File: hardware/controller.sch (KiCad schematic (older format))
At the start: 76 parts, among them J1 USB_B_Micro, Q1 AO3402, Q2 AO3401A, Q3 AO3402, SW1 SW_Push_NO_NC_LED, SW10 SW_Push_NO_NC_LED, SW11 SW_Push_NO_NC_LED, SW12 SW_Push_NO_NC_LED, SW13 SW_Push_NO_NC_LED, SW14 SW_Push_NO_NC_LED, SW15 SW_Push_NO_NC_LED, SW16 SW_Push_NO_NC_LED, SW2 SW_Push_NO_NC_LED, SW3 SW_Push_NO_NC_LED, SW4 SW_Push_NO_NC_LED, SW5 SW_Push_NO_NC_LED, SW6 SW_Push_NO_NC_LED, SW7 SW_Push_NO_NC_LED, SW8 SW_Push_NO_NC_LED, SW9 SW_Push_NO_NC_LED, U1 ESP-12F, U2 ME6211C33M5G, U3 MCP23017_SS, U4 CH340C, U5 PCA9685PW

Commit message: use ATmega8, add PCB (before automatic rounting)
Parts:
- removed C10: 10u, Capacitor_SMD:C_0805_2012Metric, symbol Device:C_Small
- removed C4: 1u, Capacitor_SMD:C_0805_2012Metric, symbol Device:C_Small
- removed H2, H3: MountingHole_Pad, MountingHole:MountingHole_3.5mm_Pad_Via, symbol Mechanical:MountingHole_Pad
- removed Q2: AO3401A, Package_TO_SOT_SMD:SOT-23, symbol Device:Q_PMOS_GSD
- removed R1, R2: 10k, Resistor_SMD:R_0805_2012Metric, symbol Device:R
- removed R10, R11, R12, R13, R14, R15, R16, R17, R18, R19, R20, R21, R22, R24, R25, R7, R8, R9: 470, Resistor_SMD:R_0805_2012Metric, symbol Device:R
- removed TP1: TXD, TestPoint:TestPoint_Loop_D1.80mm_Drill1.0mm_Beaded, symbol Connector:TestPoint
- removed TP2: RXD, TestPoint:TestPoint_Loop_D1.80mm_Drill1.0mm_Beaded, symbol Connector:TestPoint
- removed TP3: GPIO0, TestPoint:TestPoint_Loop_D1.80mm_Drill1.0mm_Beaded, symbol Connector:TestPoint
- removed TP4: ~RST, TestPoint:TestPoint_Loop_D1.80mm_Drill1.0mm_Beaded, symbol Connector:TestPoint
- removed TP5: ~RTS, TestPoint:TestPoint_Loop_D1.80mm_Drill1.0mm_Beaded, symbol Connector:TestPoint
- removed TP6: ~DTR, TestPoint:TestPoint_Loop_D1.80mm_Drill1.0mm_Beaded, symbol Connector:TestPoint
- removed U1: ESP-12F, RF_Module:ESP-12E, symbol RF_Module:ESP-12F
- removed U2: ME6211C33M5G, Package_TO_SOT_SMD:SOT-23-5, symbol Regulator_Linear:TLV75533PDBV
- added C2, C5: 100n, Capacitor_SMD:C_0805_2012Metric, symbol Device:C_Small
- added H2, H3, H4: MountingHole, MountingHole:MountingHole_3.5mm, symbol Mechanical:MountingHole
- added J2: AVR-ISP-6, Connector_PinHeader_2.54mm:PinHeader_2x03_P2.54mm_Vertical, symbol Connector:AVR-ISP-6
- added Q10, Q11, Q12, Q13, Q14, Q15, Q16, Q2, Q4, Q5, Q6, Q7, Q8, Q9: AO3402, Package_TO_SOT_SMD:SOT-23, symbol Device:Q_NMOS_GSD
- added U2: ATmega328-AU, Package_QFP:TQFP-32_7x7mm_P0.8mm, symbol MCU_Microchip_ATmega:ATmega328-AU
- added Y1: 14.7456 Mhz, Crystal:Crystal_SMD_HC49-SD, symbol Device:Crystal
- C1: footprint Capacitor_SMD:C_0805_2012Metric -> Capacitor_THT:C_Disc_D6.0mm_W2.5mm_P5.00mm
- C3: value 1u -> 100n
- C6: value 10u -> 100n
- C7: value 10u -> 22p
- C8: value 100n -> 22p
- H1: value MountingHole_Pad -> MountingHole; footprint MountingHole:MountingHole_3.5mm_Pad_Via -> MountingHole:MountingHole_3.5mm; symbol Mechanical:MountingHole_Pad -> Mechanical:MountingHole
- renumbered C9 to C10, C2 to C4, C5 to C9, R23 to R1, R6 to R2, TP7 to TP1, TP8 to TP2, TP9 to TP3, TP10 to TP4, TP11 to TP5, TP12 to TP6, U4 to U1, U5 to U4
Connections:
- net labels added: BTNx0, BTNx1, BTNx2, BTNx3, BTNx4, BTNx5, BTNx6, BTNx7, BTNx8, BTNx9, BTNxA, BTNxB, BTNxC, BTNxD, BTNxE, BTNxF, INTA, INTB, LEDx0, LEDx1, LEDx2, LEDx3, LEDx4, LEDx5, LEDx6, LEDx7, LEDx8, LEDx9, LEDxA, LEDxB, LEDxC, LEDxD, LEDxE, LEDxF, MCP23017.~RESET, MISO, MOSI, PCA9685.~OE, SCK, XTAL1, XTAL2
- net labels removed: +3V3, BTNx0#-, BTNx0#C, BTNx1#-, BTNx1#C, BTNx2#-, BTNx2#C, BTNx3#-, BTNx3#C, BTNx4#-, BTNx4#C, BTNx5#-, BTNx5#C, BTNx6#-, BTNx6#C, BTNx7#-, BTNx7#C, BTNx8#-, BTNx8#C, BTNx9#-, BTNx9#C, BTNxA#-, BTNxA#C, BTNxB#-, BTNxB#C, BTNxC#-, BTNxC#C, BTNxD#-, BTNxD#C, BTNxE#-, BTNxE#C, BTNxF#-, BTNxF#C, GPIO0, ~DTR, ~OE, ~RTS
- wire segments 353 -> 290
- no-connect marks 34 -> 40
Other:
- note removed: "nRTS / nDTR -> nRST / GPIO0\nL / L -> H / H\nL / H -> L / H\nH / L -> H / L\nH / H -> H / H"
- moved on the sheet: C10, C4, C9, F1, J1, R1, R2, TP1, TP2, TP3, TP4, TP5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

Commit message: fix pull-up resistors: MCP23017.~RESET is always pulled high; PCA9685.~OE is pulled high but can be driven low by PC2
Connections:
- wire segments 290 -> 289
- no-connect marks 40 -> 41
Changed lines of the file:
@@
 Wire Wire Line
 	6550 2950 6600 2950
-Text GLabel 6600 2950 2    33   Output ~ 0
-MCP23017.~RESET
 Wire Wire Line
 	4850 4050 4900 4050
-Text GLabel 6600 3050 2    33   Output ~ 0
-PCA9685.~OE
-Wire Wire Line
-	6550 3050 6600 3050
 Wire Wire Line
 	3650 1750 3700 1750
@@
 Wire Wire Line
 	7250 4150 7300 4150
-$Comp
-L power:GND #PWR073
-U 1 1 5E980FCC
-P 10100 5500
-F 0 "#PWR073" H 10100 5250 50  0001 C CNN
-F 1 "GND" H 10105 5327 50  0000 C CNN
-F 2 "" H 10100 5500 50  0001 C CNN
-F 3 "" H 10100 5500 50  0001 C CNN
-	1    10100 5500
-	1    0    0    -1
-$EndComp
 Wire Wire Line
 	10400 5500 10400 5450
@@
 Wire Wire Line
 	9800 5450 9800 5500
-Wire Wire Line
-	9200 5450 9200 5500
-Wire Wire Line
-	9500 5450 9500 5500
-Wire Wire Line
-	10100 5500 10100 5450
 $Comp
 L power:+5V #PWR074
@@
 	1    0    0    -1
 $EndComp
-Wire Wire Line
-	10100 5100 10100 5150
-$Comp
-L Device:R R4
-U 1 1 612CD065
-P 10100 5300
-F 0 "R4" H 10030 5254 50  0000 R CNN
-F 1 "10k" H 10030 5345 50  0000 R CNN
-F 2 "Resistor_SMD:R_0805_2012Metric" V 10030 5300 50  0001 C CNN
-F 3 "~" H 10100 5300 50  0001 C CNN
-	1    10100 5300
-	-1   0    0    1
-$EndComp
-Text GLabel 10100 5100 1    33   UnSpc ~ 0
-MCP23017.~RESET
 Wire Wire Line
 	9800 5100 9800 5150
@@
 ~RST
 $Comp
-L power:+5V #PWR069
-U 1 1 5ED52F54
-P 9200 5100
-F 0 "#PWR069" H 9200 4950 50  0001 C CNN
-F 1 "+5V" H 9215 5273 50  0000 C CNN
-F 2 "" H 9200 5100 50  0001 C CNN
-F 3 "" H 9200 5100 50  0001 C CNN
-	1    9200 5100
-	1    0    0    -1
-$EndComp
-$Comp
-L power:+5V #PWR070
-U 1 1 5ED51F9D
-P 9500 5100
-F 0 "#PWR070" H 9500 4950 50  0001 C CNN
-F 1 "+5V" H 9515 5273 50  0000 C CNN
-F 2 "" H 9500 5100 50  0001 C CNN
-F 3 "" H 9500 5100 50  0001 C CNN
-	1    9500 5100
-	1    0    0    -1
-$EndComp
-Text GLabel 9500 5500 3    50   UnSpc ~ 0
-SDA
-Text GLabel 9200 5500 3    50   UnSpc ~ 0
-SCL
-Wire Wire Line
-	9200 5100 9200 5150
-Wire Wire Line
-	9500 5100 9500 5150
+L Device:C_Small C7
+U 1 1 601D1409
+P 7300 4350
+F 0 "C7" H 7415 4396 50  0000 L CNN
+F 1 "22p" H 7415 4305 50  0000 L CNN
+F 2 "Capacitor_SMD:C_0805_2012Metric" H 7338 4200 50  0001 C CNN
+F 3 "~" H 7300 4350 50  0001 C CNN
+	1    7300 4350
+	1    0    0    -1
+$EndComp
+Text GLabel 6600 2550 2    50   Output ~ 0
+XTAL2
+Wire Wire Line
+	6550 2550 6600 2550
+Text GLabel 6600 2450 2    50   Input ~ 0
+XTAL1
+Wire Wire Line
+	6600 2450 6550 2450
+$Comp
+L Device:R R2
+U 1 1 5E2A6C3C
+P 9500 5300
+F 0 "R2" H 9430 5254 50  0000 R CNN
+F 1 "1k5" H 9430 5345 50  0000 R CNN
+F 2 "Resistor_SMD:R_0805_2012Metric" V 9430 5300 50  0001 C CNN
+F 3 "~" H 9500 5300 50  0001 C CNN
+	1    9500 5300
+	-1   0    0    1
+$EndComp
 $Comp
 L Device:R R1
@@
 	-1   0    0    1
 $EndComp
-$Comp
-L Device:R R2
-U 1 1 5E2A6C3C
-P 9500 5300
-F 0 "R2" H 9430 5254 50  0000 R CNN
-F 1 "1k5" H 9430 5345 50  0000 R CNN
-F 2 "Resistor_SMD:R_0805_2012Metric" V 9430 5300 50  0001 C CNN
-F 3 "~" H 9500 5300 50  0001 C CNN
-	1    9500 5300
-	-1   0    0    1
-$EndComp
-$Comp
-L Device:C_Small C7
-U 1 1 601D1409
-P 7300 4350
-F 0 "C7" H 7415 4396 50  0000 L CNN
-F 1 "22p" H 7415 4305 50  0000 L CNN
-F 2 "Capacitor_SMD:C_0805_2012Metric" H 7338 4200 50  0001 C CNN
-F 3 "~" H 7300 4350 50  0001 C CNN
-	1    7300 4350
-	1    0    0    -1
-$EndComp
-Text GLabel 6600 2550 2    50   Output ~ 0
-XTAL2
-Wire Wire Line
-	6550 2550 6600 2550
-Text GLabel 6600 2450 2    50   Input ~ 0
-XTAL1
-Wire Wire Line
-	6600 2450 6550 2450
+Wire Wire Line
+	9500 5100 9500 5150
+Wire Wire Line
+	9200 5100 9200 5150
+Text GLabel 9200 5500 3    50   UnSpc ~ 0
+SCL
+Text GLabel 9500 5500 3    50   UnSpc ~ 0
+SDA
+$Comp
+L power:+5V #PWR070
+U 1 1 5ED51F9D
+P 9500 5100
+F 0 "#PWR070" H 9500 4950 50  0001 C CNN
+F 1 "+5V" H 9515 5273 50  0000 C CNN
+F 2 "" H 9500 5100 50  0001 C CNN
+F 3 "" H 9500 5100 50  0001 C CNN
+	1    9500 5100
+	1    0    0    -1
+$EndComp
+$Comp
+L power:+5V #PWR069
+U 1 1 5ED52F54
+P 9200 5100
+F 0 "#PWR069" H 9200 4950 50  0001 C CNN
+F 1 "+5V" H 9215 5273 50  0000 C CNN
+F 2 "" H 9200 5100 50  0001 C CNN
+F 3 "" H 9200 5100 50  0001 C CNN
+	1    9200 5100
+	1    0    0    -1
+$EndComp
+Wire Wire Line
+	9500 5450 9500 5500
+Wire Wire Line
+	9200 5450 9200 5500
+Text GLabel 6600 2950 2    33   Output ~ 0
+PCA9685.~OE
+Wire Wire Line
+	10100 5100 10100 5150
+Wire Wire Line
+	10100 5500 10100 5450
+$Comp
+L Device:R R4
+U 1 1 612CD065
+P 10100 5300
+F 0 "R4" H 10030 5254 50  0000 R CNN
+F 1 "10k" H 10030 5345 50  0000 R CNN
+F 2 "Resistor_SMD:R_0805_2012Metric" V 10030 5300 50  0001 C CNN
+F 3 "~" H 10100 5300 50  0001 C CNN
+	1    10100 5300
+	-1   0    0    -1
+$EndComp
+Text GLabel 10100 5500 3    33   UnSpc ~ 0
+MCP23017.~RESET
+$Comp
+L power:+5V #PWR?
+U 1 1 5EA7F4C0
+P 10100 5100
+F 0 "#PWR?" H 10100 4950 50  0001 C CNN
+F 1 "+5V" H 10115 5273 50  0000 C CNN
+F 2 "" H 10100 5100 50  0001 C CNN
+F 3 "" H 10100 5100 50  0001 C CNN
+	1    10100 5100
+	1    0    0    -1
+$EndComp
+NoConn ~ 6550 3050
 $EndSCHEMATC

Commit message: update schematic with separate connectors for LEDs and buttons
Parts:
- removed SW1, SW10, SW11, SW12, SW13, SW14, SW15, SW16, SW2, SW3, SW4, SW5, SW6, SW7, SW8, SW9: SW_Push_NO_NC_LED, Connector_Molex:Molex_PicoBlade_53047-0510_1x05_P1.25mm_Vertical, symbol controller:SW_Push_NO_NC_LED
- added J10, J11, J12, J13, J14, J15, J16, J17, J18, J3, J4, J5, J6, J7, J8, J9: Conn_01x02_Male, Connector_Molex:Molex_PicoBlade_53047-0210_1x02_P1.25mm_Vertical, symbol Connector:Conn_01x02_Male
- added J19, J20, J21, J22, J23, J24, J25, J26, J27, J28, J29, J30, J31, J32, J33, J34: Conn_01x03_Male, Connector_Molex:Molex_PicoBlade_53047-0310_1x03_P1.25mm_Vertical, symbol Connector:Conn_01x03_Male
- renumbered C3 to C1, C8 to C10, C4 to C2, C5 to C3, C6 to C4, C9 to C5, C10 to C6, C2 to C7, C1 to C8, C7 to C9, U4 to U2, U2 to U4
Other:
- moved on the sheet: C1, C10, C7, C8, C9, F1, H1, H2, H3, H4, J1, J2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

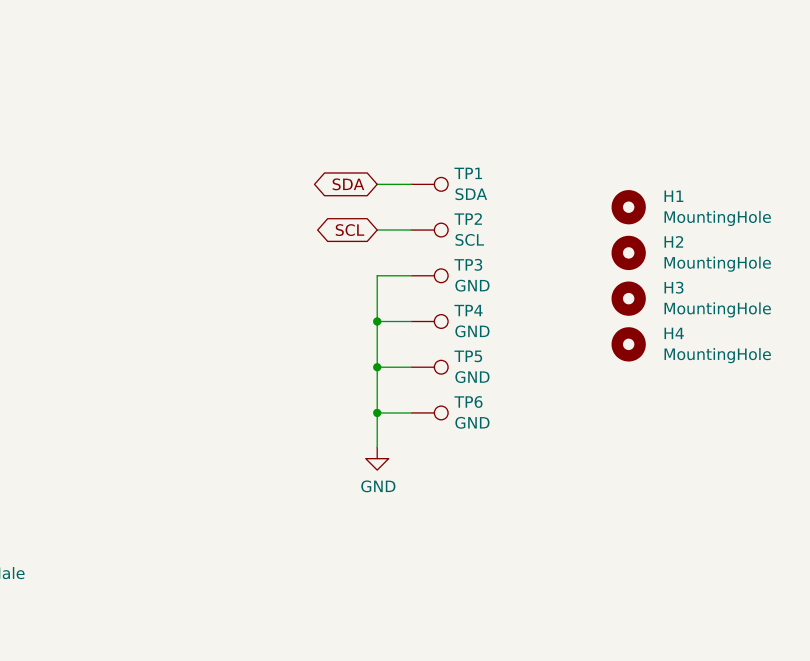
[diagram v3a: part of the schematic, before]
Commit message: remove test points
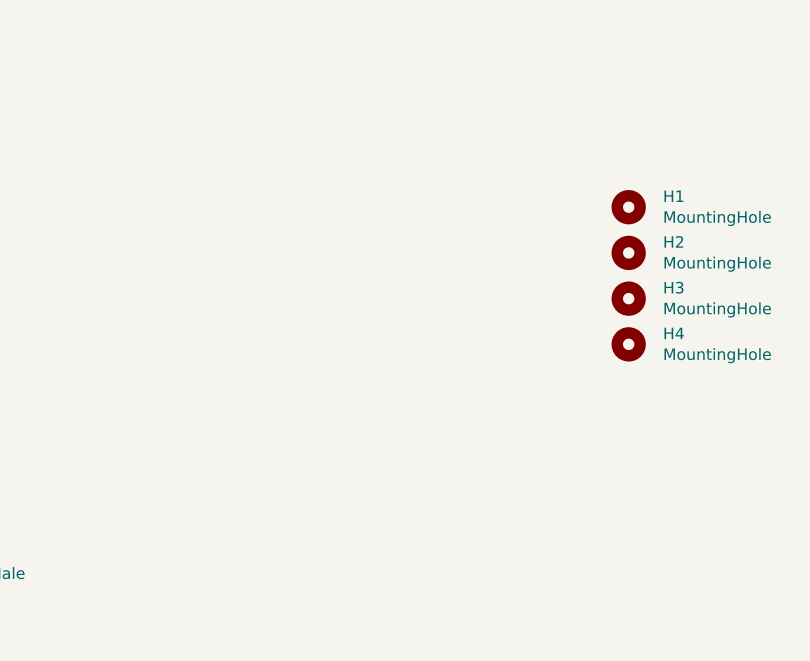
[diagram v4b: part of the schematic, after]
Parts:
- removed TP1: SDA, TestPoint:TestPoint_Loop_D1.80mm_Drill1.0mm_Beaded, symbol Connector:TestPoint
- removed TP2: SCL, TestPoint:TestPoint_Loop_D1.80mm_Drill1.0mm_Beaded, symbol Connector:TestPoint
- removed TP3, TP4, TP5, TP6: GND, TestPoint:TestPoint_Loop_D1.80mm_Drill1.0mm_Beaded, symbol Connector:TestPoint
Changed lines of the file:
@@
 Wire Wire Line
 	10050 3350 10050 3250
-Wire Wire Line
-	11850 8350 11850 8550
-Text GLabel 11850 7750 0    50   BiDi ~ 0
-SCL
-Text GLabel 11850 7550 0    50   BiDi ~ 0
-SDA
-$Comp
-L Connector:TestPoint TP2
-U 1 1 5E3F50CB
-P 12000 7750
-F 0 "TP2" V 11954 7938 50  0000 L CNN
-F 1 "SCL" V 12045 7938 50  0000 L CNN
-F 2 "TestPoint:TestPoint_Loop_D1.80mm_Drill1.0mm_Beaded" H 12200 7750 50  0001 C CNN
-F 3 "~" H 12200 7750 50  0001 C CNN
-	1    12000 7750
-	0    1    1    0
-$EndComp
-$Comp
-L Connector:TestPoint TP5
-U 1 1 5E7B1239
-P 12000 8350
-F 0 "TP5" V 11954 8538 50  0000 L CNN
-F 1 "GND" V 12045 8538 50  0000 L CNN
-F 2 "TestPoint:TestPoint_Loop_D1.80mm_Drill1.0mm_Beaded" H 12200 8350 50  0001 C CNN
-F 3 "~" H 12200 8350 50  0001 C CNN
-	1    12000 8350
-	0    1    1    0
-$EndComp
-Wire Wire Line
-	12000 8350 11850 8350
-Wire Wire Line
-	11850 7750 12000 7750
-Wire Wire Line
-	11850 7550 12000 7550
-$Comp
-L Connector:TestPoint TP1
-U 1 1 5E7B274E
-P 12000 7550
-F 0 "TP1" V 11954 7738 50  0000 L CNN
-F 1 "SDA" V 12045 7738 50  0000 L CNN
-F 2 "TestPoint:TestPoint_Loop_D1.80mm_Drill1.0mm_Beaded" H 12200 7550 50  0001 C CNN
-F 3 "~" H 12200 7550 50  0001 C CNN
-	1    12000 7550
-	0    1    1    0
-$EndComp
 Text Notes 11000 3650 0    50   ~ 0
 I2C Address: 0 1 0 0 (A2) (A1) (A0)
 $Comp
-L Connector:TestPoint TP6
-U 1 1 5EBCB80A
-P 12000 8550
-F 0 "TP6" V 11954 8738 50  0000 L CNN
-F 1 "GND" V 12045 8738 50  0000 L CNN
-F 2 "TestPoint:TestPoint_Loop_D1.80mm_Drill1.0mm_Beaded" H 12200 8550 50  0001 C CNN
-F 3 "~" H 12200 8550 50  0001 C CNN
-	1    12000 8550
-	0    1    1    0
-$EndComp
-Wire Wire Line
-	12000 8550 11850 8550
-$Comp
-L Connector:TestPoint TP4
-U 1 1 5E42C1D7
-P 12000 8150
-F 0 "TP4" V 11954 8338 50  0000 L CNN
-F 1 "GND" V 12045 8338 50  0000 L CNN
-F 2 "TestPoint:TestPoint_Loop_D1.80mm_Drill1.0mm_Beaded" H 12200 8150 50  0001 C CNN
-F 3 "~" H 12200 8150 50  0001 C CNN
-	1    12000 8150
-	0    1    1    0
-$EndComp
-$Comp
-L Connector:TestPoint TP3
-U 1 1 5E42D41F
-P 12000 7950
-F 0 "TP3" V 11954 8138 50  0000 L CNN
-F 1 "GND" V 12045 8138 50  0000 L CNN
-F 2 "TestPoint:TestPoint_Loop_D1.80mm_Drill1.0mm_Beaded" H 12200 7950 50  0001 C CNN
-F 3 "~" H 12200 7950 50  0001 C CNN
-	1    12000 7950
-	0    1    1    0
-$EndComp
-Wire Wire Line
-	11850 8350 11850 8150
-Wire Wire Line
-	11850 7950 12000 7950
-Connection ~ 11850 8350
-Wire Wire Line
-	12000 8150 11850 8150
-Connection ~ 11850 8150
-Wire Wire Line
-	11850 8150 11850 7950
-$Comp
-L power:GND #PWR068
-U 1 1 5E500BD6
-P 11850 8700
-F 0 "#PWR068" H 11850 8450 50  0001 C CNN
-F 1 "GND" H 11855 8527 50  0000 C CNN
-F 2 "" H 11850 8700 50  0001 C CNN
-F 3 "" H 11850 8700 50  0001 C CNN
-	1    11850 8700
-	1    0    0    -1
-$EndComp
-Wire Wire Line
-	11850 8700 11850 8550
-Connection ~ 11850 8550
-$Comp
 L power:+5V #PWR011

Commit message: create routing-friendly PCB layout and route it manually
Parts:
- removed J10, J11, J12, J13, J14, J15, J16, J17, J18, J3, J4, J5, J6, J7, J8, J9: Conn_01x02_Male, Connector_Molex:Molex_PicoBlade_53047-0210_1x02_P1.25mm_Vertical, symbol Connector:Conn_01x02_Male
- removed J20, J21, J22, J23, J24, J25, J26, J27, J28, J29, J30, J31, J32, J33, J34: Conn_01x03_Male, Connector_Molex:Molex_PicoBlade_53047-0310_1x03_P1.25mm_Vertical, symbol Connector:Conn_01x03_Male
- added J10, J11, J12, J13, J14, J15, J16, J17, J18, J4, J5, J6, J7, J8, J9: Conn_01x05_Male, Connector_JST:JST_XH_B5B-XH-A_1x05_P2.50mm_Vertical, symbol Connector:Conn_01x05_Male
- J3: renamed from J19; value Conn_01x03_Male -> Conn_01x05_Male; footprint Connector_Molex:Molex_PicoBlade_53047-0310_1x03_P1.25mm_Vertical -> Connector_JST:JST_XH_B5B-XH-A_1x05_P2.50mm_Vertical; symbol Connector:Conn_01x03_Male -> Connector:Conn_01x05_Male
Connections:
- net +5V: now also J3.5 (Pin_5), J10.5 (Pin_5), J11.5 (Pin_5), J12.5 (Pin_5), J13.5 (Pin_5), J14.5 (Pin_5), J15.5 (Pin_5), J16.5 (Pin_5), J17.5 (Pin_5), J18.5 (Pin_5), J4.5 (Pin_5), J5.5 (Pin_5), J6.5 (Pin_5), J7.5 (Pin_5), J8.5 (Pin_5), J9.5 (Pin_5)
- net BTNx0: now also J3.4 (Pin_4); no longer J3.2 (Pin_2)
- net BTNx1: now also J4.4 (Pin_4)
- net BTNx2: now also J5.4 (Pin_4)
- net BTNx3: now also J6.4 (Pin_4)
- net BTNx4: now also J7.4 (Pin_4)
- net BTNx5: now also J8.4 (Pin_4)
- net BTNx6: now also J9.4 (Pin_4)
- net BTNx7: now also J10.4 (Pin_4)
- net BTNx8: now also J11.4 (Pin_4)
- net BTNx9: now also J12.4 (Pin_4)
- net BTNxA: now also J13.4 (Pin_4)
- net BTNxB: now also J14.4 (Pin_4)
- net BTNxC: now also J15.4 (Pin_4)
- net BTNxD: now also J16.4 (Pin_4)
- net BTNxE: now also J17.4 (Pin_4)
- net BTNxF: now also J18.4 (Pin_4)
- net GND: now also J3.3 (Pin_3), J10.3 (Pin_3), J11.3 (Pin_3), J12.3 (Pin_3), J13.3 (Pin_3), J14.3 (Pin_3), J15.3 (Pin_3), J16.3 (Pin_3), J17.3 (Pin_3), J18.3 (Pin_3), J4.3 (Pin_3), J5.3 (Pin_3), J6.3 (Pin_3), J7.3 (Pin_3), J8.3 (Pin_3), J9.3 (Pin_3); no longer J3.1 (Pin_1)
- net at Q1.3 (D): now also J3.1 (Pin_1)
- net at Q2.3 (D): now also J4.1 (Pin_1)
- net at Q3.3 (D): now also J5.1 (Pin_1)
- net at Q4.3 (D): now also J6.1 (Pin_1)
- net at Q5.3 (D): now also J7.1 (Pin_1)
- net at Q6.3 (D): now also J8.1 (Pin_1)
- net at Q7.3 (D): now also J9.1 (Pin_1)
- net at Q8.3 (D): now also J10.1 (Pin_1)
- net at Q9.3 (D): now also J11.1 (Pin_1)
- net at Q10.3 (D): now also J12.1 (Pin_1)
- net at Q11.3 (D): now also J13.1 (Pin_1)
- net at Q12.3 (D): now also J14.1 (Pin_1)
- net at Q13.3 (D): now also J15.1 (Pin_1)
- net at Q14.3 (D): now also J16.1 (Pin_1)
- net at Q15.3 (D): now also J17.1 (Pin_1)
- net at Q16.3 (D): now also J18.1 (Pin_1)
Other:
- moved on the sheet: H1, H2, H3, H4, Q1, R1, R2, R3, R4, R5

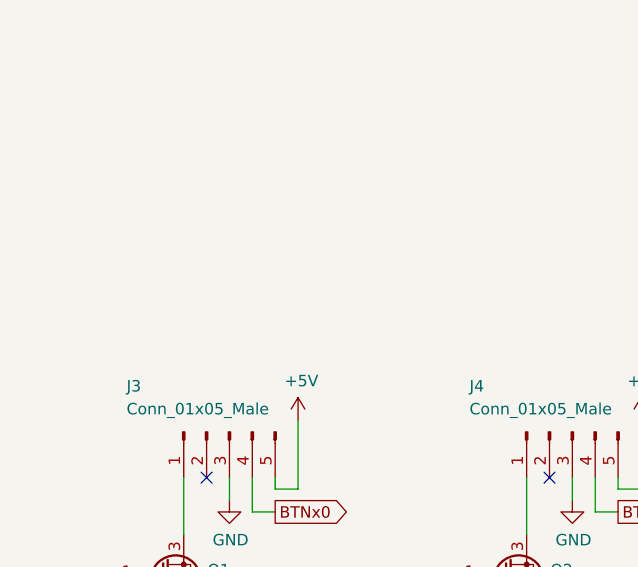
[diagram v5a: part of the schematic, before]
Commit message: change USB connector, finalize PCB shape
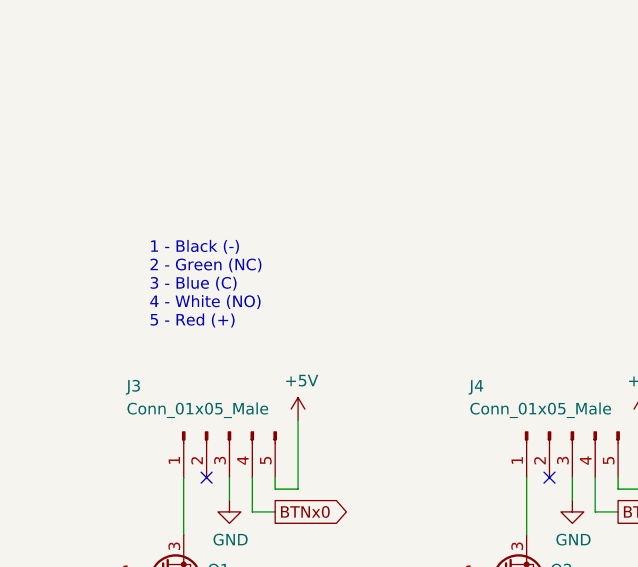
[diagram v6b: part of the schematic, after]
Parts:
- J1: footprint Connector_USB:USB_Micro-B_Amphenol_10103594-0001LF_Horizontal -> Connector_USB:USB_Micro-B_Molex-105017-0001
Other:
- note added: "1 - Black (-)\n2 - Green (NC)\n3 - Blue (C)\n4 - White (NO)\n5 - Red (+)\n"
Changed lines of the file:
@@
 F 0 "J1" H 1407 2417 50  0000 C CNN
 F 1 "USB_B_Micro" H 1407 2326 50  0000 C CNN
-F 2 "Connector_USB:USB_Micro-B_Amphenol_10103594-0001LF_Horizontal" H 1500 1900 50  0001 C CNN
+F 2 "Connector_USB:USB_Micro-B_Molex-105017-0001" H 1500 1900 50  0001 C CNN
 F 3 "~" H 1500 1900 50  0001 C CNN
 	1    1350 1950
@@
 	0    -1   1    0
 $EndComp
+Text Notes 1250 6300 0    50   ~ 0
+1 - Black (-)\n2 - Green (NC)\n3 - Blue (C)\n4 - White (NO)\n5 - Red (+)\n
 $EndSCHEMATC

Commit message: fix assignment of SCL and SDA pins on ATmega328p
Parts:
- U4: value ATmega328-AU -> ATmega328P-MU; symbol MCU_Microchip_ATmega:ATmega328-AU -> MCU_Microchip_ATmega:ATmega328P-MU
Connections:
- net GND: now also U4.33 (GND)
- net SCL: now also U4.28 (PC5); no longer U4.27 (PC4)
- net SDA: now also U4.27 (PC4); no longer U4.28 (PC5)
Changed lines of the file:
@@
 Wire Wire Line
 	7850 2000 7850 2050
-$Comp
-L MCU_Microchip_ATmega:ATmega328-AU U4
-U 1 1 5E9057B7
-P 5950 3050
-F 0 "U4" H 5950 3100 50  0000 C CNN
-F 1 "ATmega328-AU" H 5950 3000 50  0000 C CNN
-F 2 "Package_QFP:TQFP-32_7x7mm_P0.8mm" H 5950 3050 50  0001 C CIN
-F 3 "http://ww1.microchip.com/downloads/en/DeviceDoc/ATmega328_P%20AVR%20MCU%20with%20picoPower%20Technology%20Data%20Sheet%2040001984A.pdf" H 5950 3050 50  0001 C CNN
-	1    5950 3050
-	1    0    0    -1
-$EndComp
 Wire Wire Line
 	10050 2650 10100 2650
+Text GLabel 6600 3250 2    50   BiDi ~ 0
+SCL
+Wire Wire Line
+	6550 3150 6600 3150
 Text GLabel 6600 3150 2    50   BiDi ~ 0
-SCL
-Wire Wire Line
-	6550 3150 6600 3150
-Text GLabel 6600 3250 2    50   BiDi ~ 0
 SDA
 Wire Wire Line
@@
 Text Notes 1250 6300 0    50   ~ 0
 1 - Black (-)\n2 - Green (NC)\n3 - Blue (C)\n4 - White (NO)\n5 - Red (+)\n
+$Comp
+L MCU_Microchip_ATmega:ATmega328P-MU U4
+U 1 1 5E9057B7
+P 5950 3050
+F 0 "U4" H 5950 3100 50  0000 C CNN
+F 1 "ATmega328P-MU" H 5950 3000 50  0000 C CNN
+F 2 "Package_QFP:TQFP-32_7x7mm_P0.8mm" H 5950 3050 50  0001 C CIN
+F 3 "http://ww1.microchip.com/downloads/en/DeviceDoc/Atmel-7810-Automotive-Microcontrollers-ATmega328P_Datasheet.pdf" H 5950 3050 50  0001 C CNN
+	1    5950 3050
+	1    0    0    -1
+$EndComp
 $EndSCHEMATC

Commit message: use 36pF capacitors for crystal
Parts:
- C10, C9: value 22p -> 36p
- U4: value ATmega328P-MU -> ATmega328P-AU; symbol MCU_Microchip_ATmega:ATmega328P-MU -> MCU_Microchip_ATmega:ATmega328P-AU
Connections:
- net GND: no longer U4.33 (GND)
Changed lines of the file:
@@
 P 8000 4000
 F 0 "C10" H 8115 4046 50  0000 L CNN
-F 1 "22p" H 8115 3955 50  0000 L CNN
+F 1 "36p" H 8115 3955 50  0000 L CNN
 F 2 "Capacitor_SMD:C_0805_2012Metric" H 8038 3850 50  0001 C CNN
 F 3 "~" H 8000 4000 50  0001 C CNN
@@
 P 7600 4000
 F 0 "C9" H 7715 4046 50  0000 L CNN
-F 1 "22p" H 7715 3955 50  0000 L CNN
+F 1 "36p" H 7715 3955 50  0000 L CNN
 F 2 "Capacitor_SMD:C_0805_2012Metric" H 7638 3850 50  0001 C CNN
 F 3 "~" H 7600 4000 50  0001 C CNN
@@
 1 - Black (-)\n2 - Green (NC)\n3 - Blue (C)\n4 - White (NO)\n5 - Red (+)\n
 $Comp
-L MCU_Microchip_ATmega:ATmega328P-MU U4
+L MCU_Microchip_ATmega:ATmega328P-AU U4
 U 1 1 5E9057B7
 P 5950 3050
 F 0 "U4" H 5950 3100 50  0000 C CNN
-F 1 "ATmega328P-MU" H 5950 3000 50  0000 C CNN
+F 1 "ATmega328P-AU" H 5950 3000 50  0000 C CNN
 F 2 "Package_QFP:TQFP-32_7x7mm_P0.8mm" H 5950 3050 50  0001 C CIN
 F 3 "http://ww1.microchip.com/downloads/en/DeviceDoc/Atmel-7810-Automotive-Microcontrollers-ATmega328P_Datasheet.pdf" H 5950 3050 50  0001 C CNN
